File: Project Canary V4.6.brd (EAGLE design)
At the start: 127 x 63.5 mm, 61 parts, among them IC2 ATMEGA324PA

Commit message: Added ground to pin 5, (bottom right)
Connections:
- net GND: now also BME280-HEADER.5
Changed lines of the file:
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@@
 <?xml version="1.0" encoding="utf-8"?>
 <!DOCTYPE eagle SYSTEM "eagle.dtd">
-<eagle version="9.2.1">
+<eagle version="8.4.1">
 <drawing>
 <settings>
@@
 <param name="checkRestrict" value="1"/>
 <param name="checkStop" value="0"/>
-<param name="checkValues" value="0"/>
-<param name="checkNames" value="1"/>
-<param name="checkWireStubs" value="1"/>
-<param name="checkPolygonWidth" value="0"/>
 <param name="useDiameter" value="13"/>
 <param name="maxErrors" value="50"/>
@@
 <wire x1="77.597" y1="43.18" x2="76.92" y2="43.18" width="0.1524" layer="1"/>
 <contactref element="R12" pad="2"/>
+<contactref element="BME280-HEADER" pad="5"/>
 </signal>
 <signal name="N$1">
@@
 </signal>
 </signals>
-<mfgpreviewcolors>
-<mfgpreviewcolor name="soldermaskcolor" color="0xC8008000"/>
-<mfgpreviewcolor name="silkscreencolor" color="0xFFFEFEFE"/>
-<mfgpreviewcolor name="backgroundcolor" color="0xFF282828"/>
-<mfgpreviewcolor name="coppercolor" color="0xFFFFBF00"/>
-<mfgpreviewcolor name="substratecolor" color="0xFF786E46"/>
-</mfgpreviewcolors>
 </board>
 </drawing>

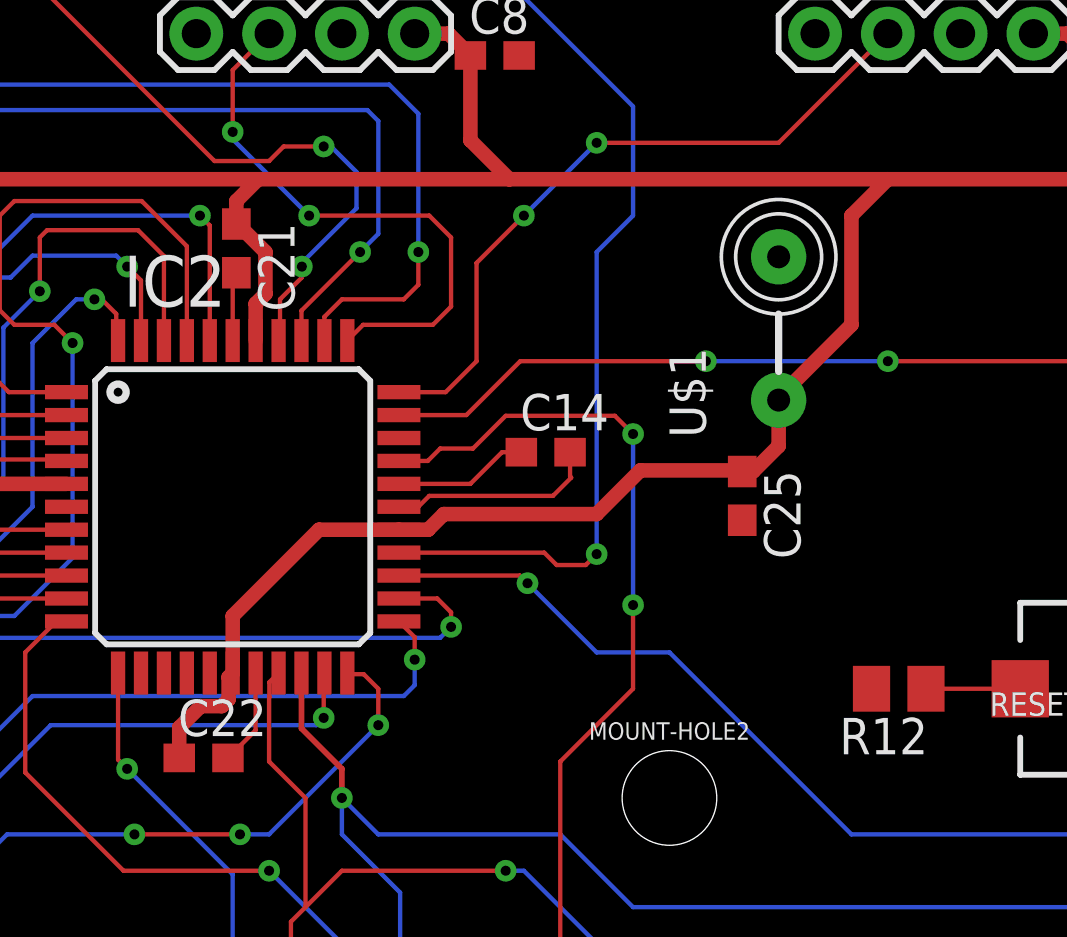
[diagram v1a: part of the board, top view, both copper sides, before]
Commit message: Fixed the Ferrite Bead and smoothed out wires
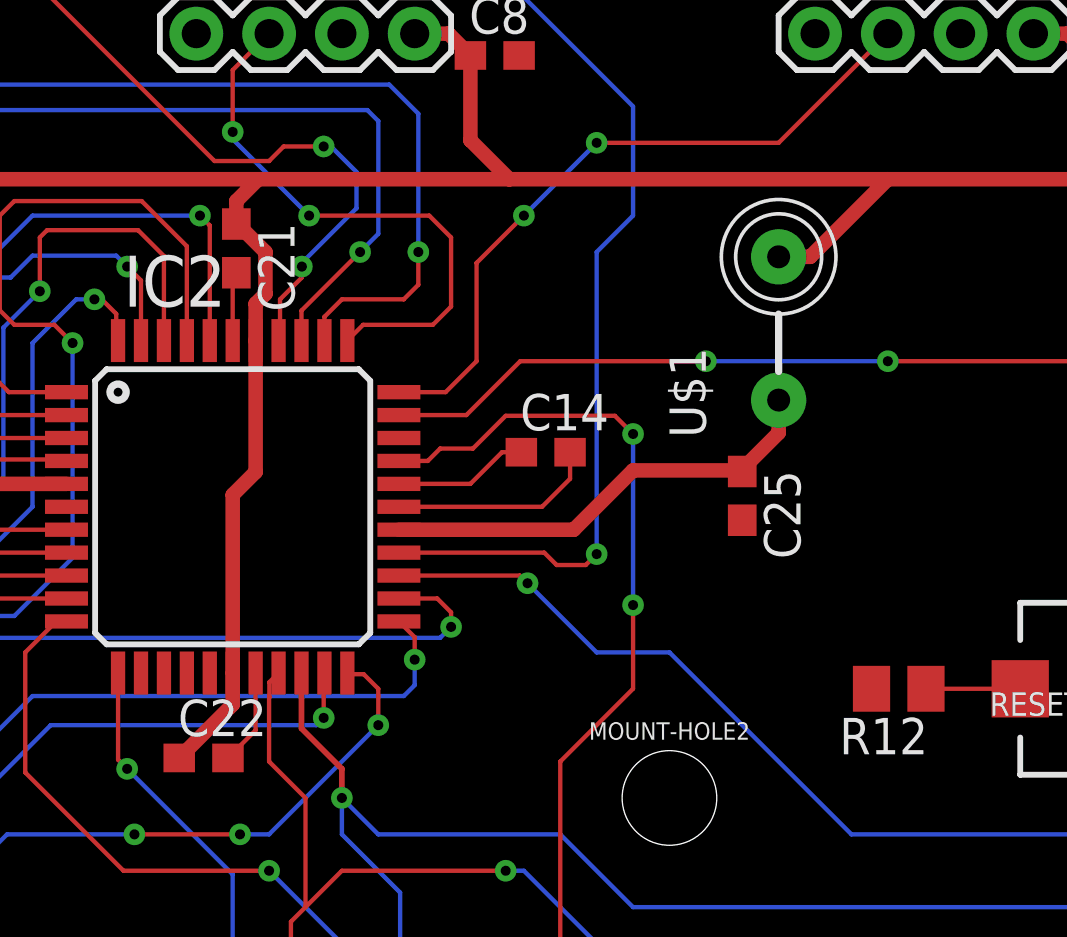
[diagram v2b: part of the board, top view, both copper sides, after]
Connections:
- net 5V: now also U$1.P$2; no longer C25.1, IC2.27, U$1.P$1
- net N$9: now also C25.1, IC2.27, U$1.P$1; no longer U$1.P$2
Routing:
- net 5V: track 351.5 -> 333.5 mm
- net N$9: track 0.00 -> 15.8 mm
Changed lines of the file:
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@@
 <setting verticaltext="up"/>
 </settings>
-<grid distance="50" unitdist="mil" unit="mil" style="lines" multiple="1" display="yes" altdistance="5" altunitdist="mil" altunit="mil"/>
+<grid distance="5" unitdist="mil" unit="mil" style="lines" multiple="1" display="yes" altdistance="1" altunitdist="mil" altunit="mil"/>
 <layers>
 <layer number="1" name="Top" color="4" fill="1" visible="yes" active="yes"/>
@@
 <wire x1="71.247" y1="51.347" x2="71.12" y2="51.22" width="0.1524" layer="1"/>
 <wire x1="71.12" y1="51.22" x2="71.12" y2="48.98" width="0.1524" layer="1"/>
-<wire x1="82.892" y1="45.085" x2="82.892" y2="44.235" width="0.1524" layer="1"/>
-<wire x1="82.892" y1="44.235" x2="82.931" y2="44.196" width="0.1524" layer="1"/>
-<wire x1="82.931" y1="44.196" x2="82.296" y2="43.561" width="0.1524" layer="1"/>
-<wire x1="82.296" y1="43.561" x2="77.978" y2="43.561" width="0.1524" layer="1"/>
-<wire x1="77.978" y1="43.561" x2="77.597" y2="43.18" width="0.1524" layer="1"/>
-<wire x1="77.597" y1="43.18" x2="76.92" y2="43.18" width="0.1524" layer="1"/>
 <contactref element="R12" pad="2"/>
 <contactref element="BME280-HEADER" pad="5"/>
+<wire x1="81.915" y1="43.18" x2="76.92" y2="43.18" width="0.1524" layer="1"/>
+<wire x1="82.892" y1="45.085" x2="82.892" y2="44.157" width="0.1524" layer="1"/>
+<wire x1="82.892" y1="44.157" x2="81.915" y2="43.18" width="0.1524" layer="1"/>
 </signal>
 <signal name="N$1">
@@
 <contactref element="LED2" pad="A"/>
 <contactref element="SWITCHING-REGULATOR" pad="OUT"/>
-<contactref element="IC2" pad="27"/>
-<contactref element="C25" pad="1"/>
-<contactref element="U$1" pad="P$1"/>
 <contactref element="LIDAR-HEADER" pad="1"/>
 <contactref element="C7" pad="1"/>
@@
 <wire x1="72.009" y1="54.61" x2="80.772" y2="54.61" width="0.508" layer="1"/>
 <wire x1="72.009" y1="54.61" x2="59.182" y2="54.61" width="0.508" layer="1"/>
-<wire x1="80.772" y1="54.61" x2="93.98" y2="54.61" width="0.508" layer="1"/>
+<wire x1="93.98" y1="54.61" x2="80.772" y2="54.61" width="0.508" layer="1"/>
 <wire x1="102.235" y1="54.61" x2="93.98" y2="54.61" width="0.508" layer="1"/>
 <wire x1="102.235" y1="54.61" x2="111.76" y2="54.61" width="0.508" layer="1"/>
@@
 <wire x1="113.03" y1="36.83" x2="114.3" y2="35.56" width="0.508" layer="1"/>
 <wire x1="114.3" y1="35.56" x2="115.57" y2="35.56" width="0.508" layer="1"/>
-<wire x1="92.71" y1="53.34" x2="92.71" y2="49.53" width="0.508" layer="1"/>
-<wire x1="92.71" y1="53.34" x2="93.98" y2="54.61" width="0.508" layer="1"/>
 <wire x1="29.21" y1="24.13" x2="29.21" y2="22.86" width="0.508" layer="1"/>
 <wire x1="29.21" y1="22.86" x2="29.21" y2="13.97" width="0.508" layer="1"/>
@@
 <wire x1="119.253" y1="30.646" x2="120.65" y2="29.249" width="0.508" layer="1"/>
 <wire x1="120.65" y1="29.249" x2="120.65" y2="26.67" width="0.508" layer="1"/>
-<wire x1="92.71" y1="49.53" x2="90.17" y2="46.99" width="0.508" layer="1"/>
-<wire x1="90.17" y1="46.99" x2="90.17" y2="46.903" width="0.508" layer="1"/>
-<wire x1="90.17" y1="45.3" x2="90.17" y2="46.903" width="0.508" layer="1"/>
-<wire x1="83.82" y1="42.926" x2="85.344" y2="44.45" width="0.508" layer="1"/>
-<wire x1="74.13" y1="42.38" x2="76.92" y2="42.38" width="0.508" layer="1"/>
-<wire x1="74.13" y1="42.38" x2="71.12" y2="39.37" width="0.508" layer="1"/>
-<wire x1="71.12" y1="39.37" x2="71.12" y2="37.38" width="0.508" layer="1"/>
-<wire x1="76.92" y1="42.38" x2="77.94" y2="42.38" width="0.508" layer="1"/>
-<wire x1="77.94" y1="42.38" x2="78.486" y2="42.926" width="0.508" layer="1"/>
-<wire x1="78.486" y1="42.926" x2="83.82" y2="42.926" width="0.508" layer="1"/>
 <wire x1="31.115" y1="20.955" x2="42.545" y2="20.955" width="0.508" layer="1"/>
 <wire x1="29.21" y1="22.86" x2="31.115" y2="20.955" width="0.508" layer="1"/>
-<wire x1="71.92" y1="48.98" x2="71.92" y2="50.2657125" width="0.508" layer="1"/>
-<wire x1="71.92" y1="50.2657125" x2="72.263" y2="50.6087125" width="0.508" layer="1"/>
+<wire x1="71.92" y1="50.2657125" x2="71.92" y2="48.98" width="0.508" layer="1"/>
+<wire x1="72.263" y1="50.6087125" x2="71.92" y2="50.2657125" width="0.508" layer="1"/>
 <wire x1="57.316" y1="59.69" x2="57.824" y2="59.182" width="0.508" layer="1"/>
 <wire x1="55.88" y1="59.69" x2="57.316" y2="59.69" width="0.508" layer="1"/>
@@
 <wire x1="115.609" y1="56.769" x2="113.45" y2="54.61" width="0.508" layer="1"/>
 <wire x1="43.18" y1="20.32" x2="43.18" y2="15.074" width="0.508" layer="1"/>
-<wire x1="85.344" y1="44.45" x2="88.861" y2="44.45" width="0.508" layer="1"/>
-<wire x1="88.861" y1="44.45" x2="88.9" y2="44.411" width="0.508" layer="1"/>
-<wire x1="88.9" y1="44.411" x2="89.281" y2="44.411" width="0.508" layer="1"/>
-<wire x1="89.281" y1="44.411" x2="90.17" y2="45.3" width="0.508" layer="1"/>
-<wire x1="71.12" y1="37.38" x2="70.9764" y2="37.2364" width="0.508" layer="1"/>
-<wire x1="70.9764" y1="37.2364" x2="70.9764" y2="36.4616625" width="0.508" layer="1"/>
-<wire x1="70.9764" y1="36.4616625" x2="70.7383375" y2="36.2236" width="0.508" layer="1"/>
-<wire x1="70.7383375" y1="36.2236" x2="70.0056" y2="36.2236" width="0.508" layer="1"/>
-<wire x1="69.254" y1="35.472" x2="69.254" y2="34.417" width="0.508" layer="1"/>
-<wire x1="70.0056" y1="36.2236" x2="69.254" y2="35.472" width="0.508" layer="1"/>
+<contactref element="U$1" pad="P$2"/>
+<wire x1="90.17" y1="51.903" x2="91.273" y2="51.903" width="0.508" layer="1"/>
+<wire x1="91.273" y1="51.903" x2="93.98" y2="54.61" width="0.508" layer="1"/>
+<wire x1="71.12" y1="43.5952625" x2="71.12" y2="37.38" width="0.508" layer="1"/>
+<wire x1="69.254" y1="34.417" x2="71.12" y2="36.283" width="0.508" layer="1"/>
+<wire x1="71.12" y1="36.283" x2="71.12" y2="37.38" width="0.508" layer="1"/>
+<wire x1="71.92" y1="48.98" x2="71.92" y2="44.3952625" width="0.508" layer="1"/>
+<wire x1="71.92" y1="44.3952625" x2="71.12" y2="43.5952625" width="0.508" layer="1"/>
 </signal>
 <signal name="N$2">
@@
 <wire x1="52.324" y1="41.91" x2="50.8" y2="43.434" width="0.1524" layer="1"/>
 </signal>
-<signal name="N$9">
-<contactref element="U$1" pad="P$2"/>
-</signal>
 <signal name="N$8">
 <contactref element="IC2" pad="7"/>
@@
 <wire x1="98.6" y1="36.83" x2="95.311" y2="36.83" width="0.1524" layer="1"/>
 </signal>
+<signal name="N$9">
+<contactref element="IC2" pad="27"/>
+<contactref element="U$1" pad="P$1"/>
+<contactref element="C25" pad="1"/>
+<wire x1="76.92" y1="42.38" x2="83.02" y2="42.38" width="0.508" layer="1"/>
+<wire x1="83.02" y1="42.38" x2="85.09" y2="44.45" width="0.508" layer="1"/>
+<wire x1="88.861" y1="44.45" x2="85.09" y2="44.45" width="0.508" layer="1"/>
+<wire x1="88.861" y1="44.45" x2="88.9" y2="44.411" width="0.508" layer="1"/>
+<wire x1="90.17" y1="46.903" x2="90.17" y2="45.759" width="0.508" layer="1"/>
+<wire x1="90.17" y1="45.759" x2="88.861" y2="44.45" width="0.508" layer="1"/>
+</signal>
 </signals>
